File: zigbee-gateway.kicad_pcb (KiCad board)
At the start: 2 copper layers, 80 x 52 mm, 13 parts, among them J1 Conn_01x04, J2 Conn_01x04, SW1 SW_Push, SW2 SW_Push, SW3 SW_Push, U1 ESP-12E, U2 CC2530-A1_Module

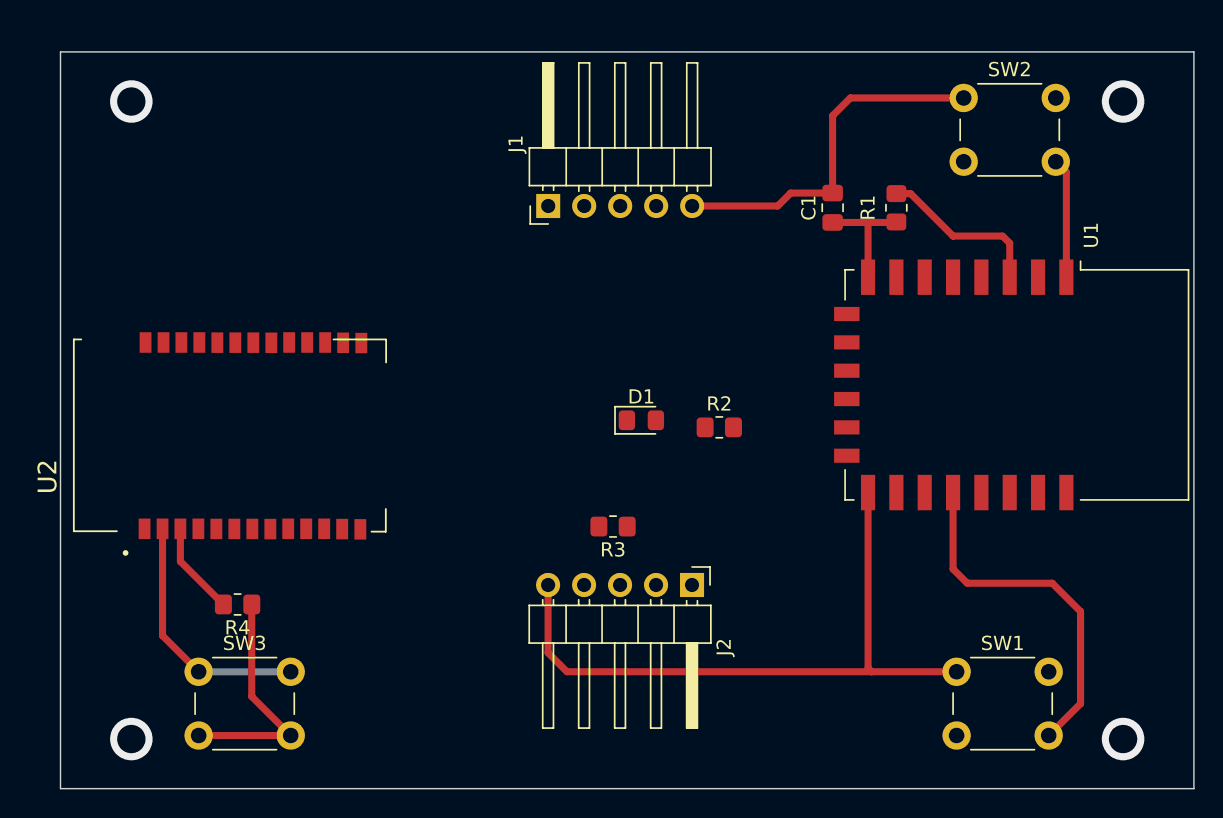
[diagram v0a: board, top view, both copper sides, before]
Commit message: ome changes performed for adding switching to the board
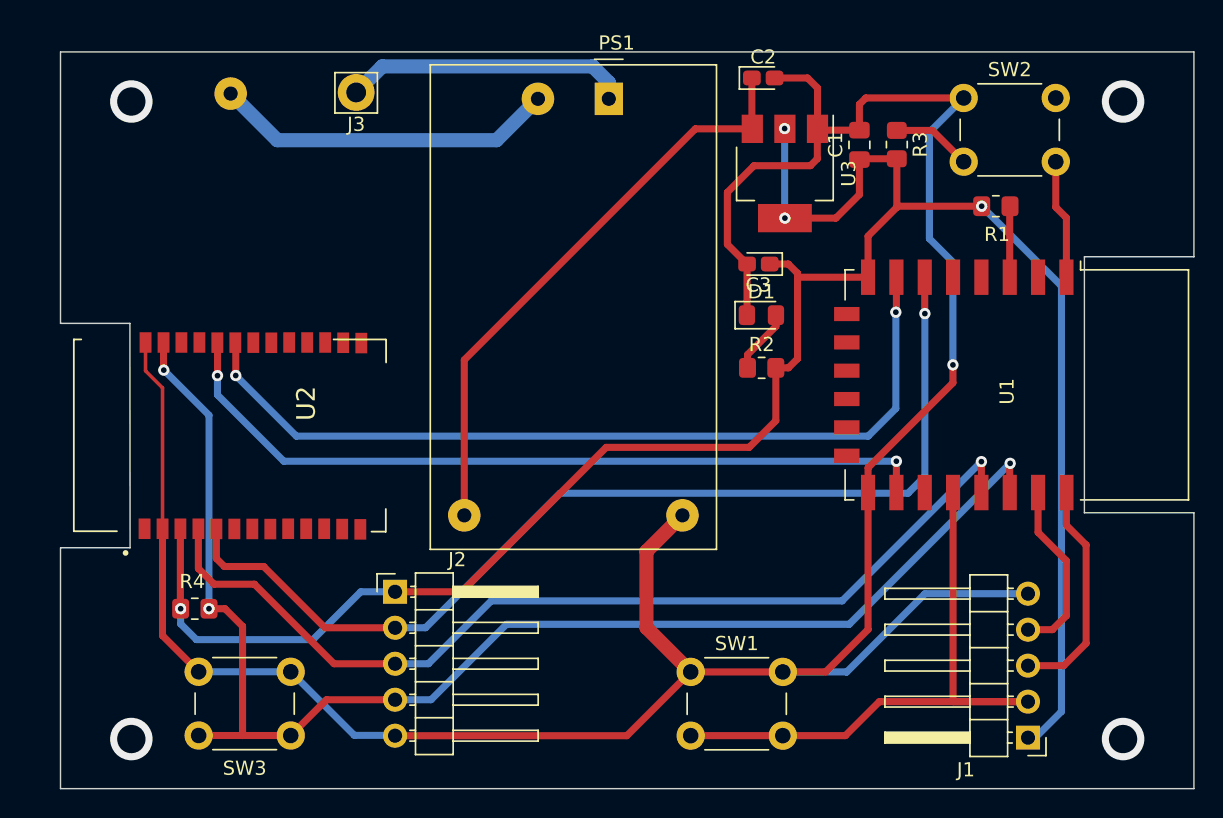
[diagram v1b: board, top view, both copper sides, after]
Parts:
- added ?: , , F.Cu at (30.5, 20.9)
- added C2: 22uF, Capacitor_Tantalum_SMD:CP_EIA-1608-10_AVX-L_Pad1.25x1.05mm_HandSolder, F.Cu at (68.1, 19.8)
- added C3: 22uF, Capacitor_Tantalum_SMD:CP_EIA-1608-10_AVX-L_Pad1.25x1.05mm_HandSolder, F.Cu at (67.8, 33.0)
- added J3: Conn_01x02_Male, Connector_Pin:Pin_D1.4mm_L8.5mm_W2.8mm_FlatFork, F.Cu at (39.4, 20.9)
- added PS1: HLK-PM01, Converter_ACDC:Converter_ACDC_HiLink_HLK-PMxx, F.Cu at (57.2, 21.3)
- added U3: AZ1117-3.3, Package_TO_SOT_SMD:SOT-223-3_TabPin2, F.Cu at (69.6, 26.6)
- moved J1 50.5 mm to (86.8, 66.4), turned to 180 degrees
- moved R3 33.6 mm to (77.5, 24.5), turned to -90 degrees
- moved J2 21.0 mm to (42.1, 56.1), turned to 0 degrees
- moved SW1 18.8 mm to (63.0, 61.8)
- moved D1 11.3 mm to (68.0, 36.6)
- moved R1 7.02 mm to (84.5, 28.9), turned to 0 degrees
- moved R2 5.16 mm to (68.0, 40.3)
- moved C1 4.83 mm to (74.9, 24.6)
- moved R4 3.03 mm to (28.0, 57.3)
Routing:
- net +3V3: track 15.0 -> 148.2 mm, vias 0 -> 4
- net GND: track 90.1 -> 189.0 mm, vias 0 -> 1
- net D1: track 16.9 -> 98.0 mm, vias 0 -> 3
- net D6: track 0.00 -> 72.6 mm, vias 0 -> 1
- net D2: track 0.00 -> 68.9 mm, vias 0 -> 1
- net D7: track 0.00 -> 60.8 mm, vias 0 -> 2
- net D8: track 0.00 -> 55.8 mm, vias 0 -> 2
- net +5V: track 0.00 -> 41.7 mm
- net Net-(J3-Pad2): track 0.00 -> 24.3 mm
- net Net-(PS1-Pad1): track 0.00 -> 20.2 mm
- net GPIO0: track 25.3 -> 44.9 mm
- net TX: track 0.00 -> 16.0 mm
- net RX: track 0.00 -> 12.6 mm
- net Net-(R1-Pad2): track 11.8 -> 5.02 mm
- net RST: track 8.46 -> 14.1 mm
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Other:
- outline, holes or cut-outs redrawn
